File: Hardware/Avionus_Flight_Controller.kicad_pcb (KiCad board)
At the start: 4 copper layers, 101.6 x 101.6 mm, 285 parts, among them J1101 PPM, J1102 iBUS, J1201 S0, J1202 S1, J1203 S2, J1204 S3, J1205 S4, J1206 S5, J1207 S6, J1208 S7, J1209 S8, J1210 S9, J1211 S10, J1212 S11, J1213 S12, J1214 S13, J1215 S14, J1216 S15, J1401 LIDAR, J201 5V_SEL, J202 E5V, J203 POWER IN, J401 STDC14, J701 SD_Card, J801 USB_C_Receptacle_USB2.0, Q1101 RE1C002UN, Q1102 RE1C002UN, Q1201 RE1C002UN, Q1202 RE1C002UN, Q1203 RE1C002UN, Q1204 RE1C002UN, Q1205 RE1C002UN, Q1206 RE1C002UN, Q1207 RE1C002UN, Q1208 RE1C002UN, Q1209 RE1C002UN, Q1210 RE1C002UN, Q1211 RE1C002UN, Q1212 RE1C002UN, Q1213 RE1C002UN, Q1214 RE1C002UN, Q1215 RE1C002UN, Q1216 RE1C002UN, Q1301 RE1C002UN, Q1501 RE1C002UN, Q1502 RE1C002UN, Q1503 RE1C002UN, Q1504 RE1C002UN, Q1505 RE1C002UN, Q201 RE1C002UN, SW1301 SW_USER, SW201 START, SW301 RESET, U1001 MAX-M10S, U1101 USBLC6-4SC6, U1201 USBLC6-4SC6, U1202 USBLC6-4SC6, U1203 USBLC6-4SC6, U1204 USBLC6-4SC6, U1401 USBLC6-4SC6, U1501 ICM-20948, U201 AP2112K-3.3, U202 AOZ1212AI, U203 AP2151W, U204 AP2112K-3.3, U205 AP2112K-1.8, U206 AP2112K-3.3, U207 AP2112K-3.3, U208 ACS714xLCTR-50A, U209 ACS714xLCTR-50A, U210 AP2171W, U301 STM32F722ZETx, U401 USBLC6-4SC6, U402 USBLC6-4SC6, U501 W25Q128JVS, U502 W25Q128JVPM, U601 W25Q128JVS, U602 W25Q128JVPM, U801 USBLC6-2SC6, U901 LAMBDA62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

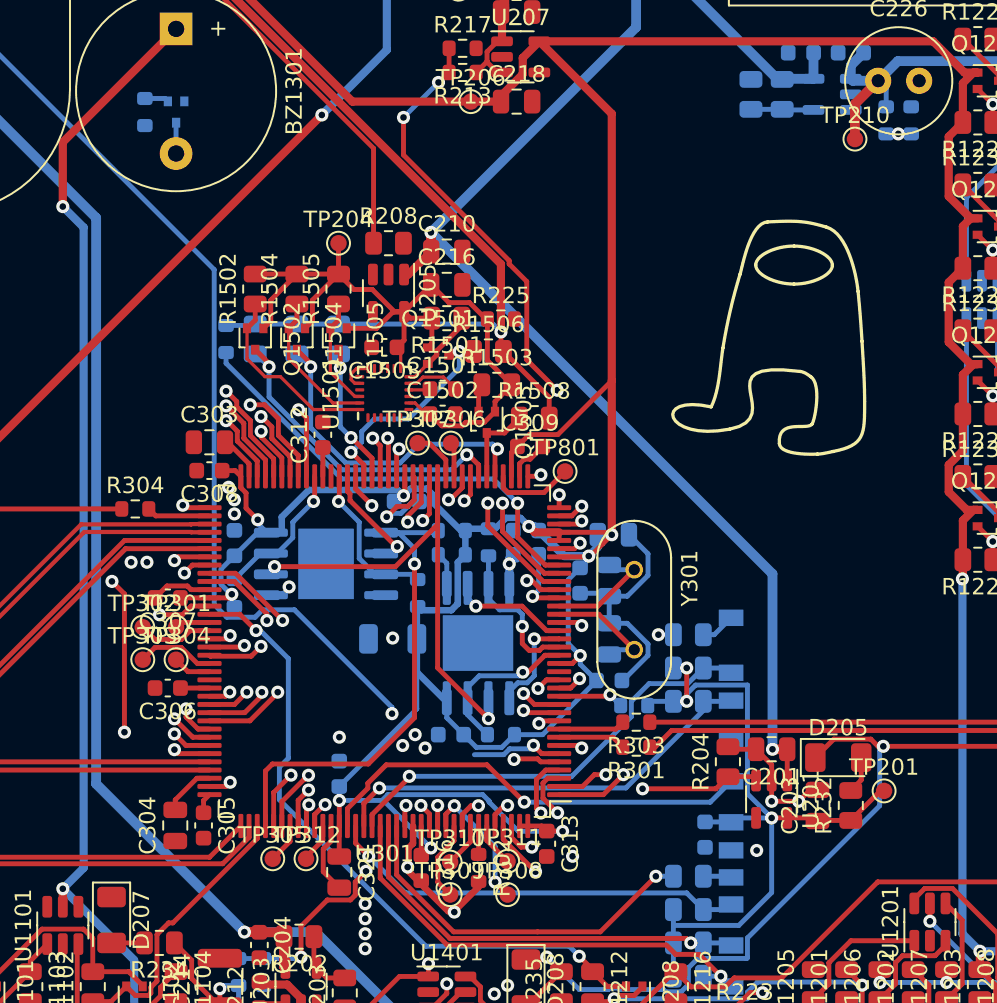
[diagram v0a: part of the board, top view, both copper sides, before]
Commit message: Schematic layout fixes
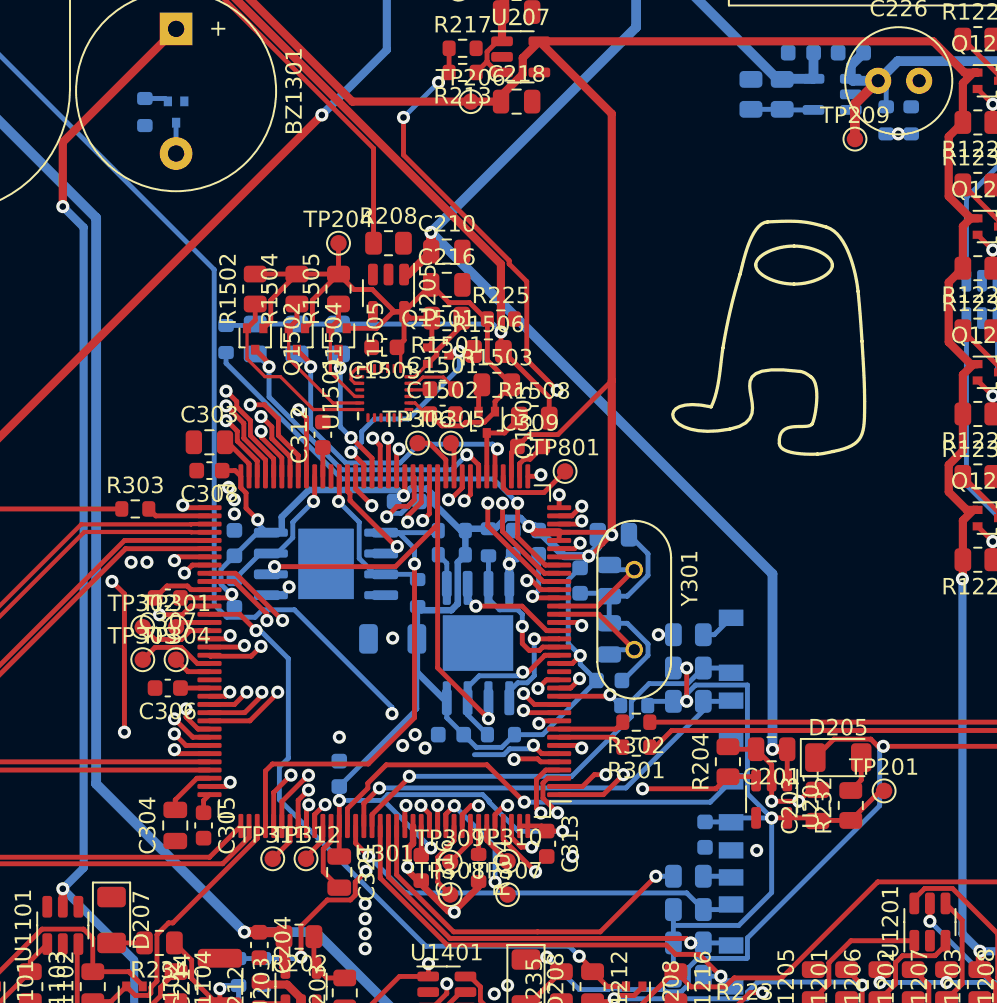
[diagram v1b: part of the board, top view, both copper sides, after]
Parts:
- renumbered R303 to R302, R304 to R303, R302 to R304, TP210 to TP209, TP306 to TP305, TP307 to TP306, TP308 to TP307, TP309 to TP308, TP310 to TP309, TP311 to TP310, TP305 to TP311
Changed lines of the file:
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@@
     (property "ki_keywords" "test point tp")
     (attr exclude_from_pos_files)
-    (fp_text reference "TP311" (at 0 -1.448) (layer "F.SilkS")
+    (fp_text reference "TP310" (at 0 -1.448) (layer "F.SilkS")
         (effects (font (size 1 1) (thickness 0.15)))
     )
@@
     (property "ki_keywords" "test point tp")
     (attr exclude_from_pos_files)
-    (fp_text reference "TP308" (at 0 -1.448) (layer "F.SilkS")
+    (fp_text reference "TP307" (at 0 -1.448) (layer "F.SilkS")
         (effects (font (size 1 1) (thickness 0.15)))
     )
@@
     (property "ki_keywords" "R resistor")
     (attr smd)
-    (fp_text reference "R304" (at 0 -1.43) (layer "F.SilkS")
+    (fp_text reference "R303" (at 0 -1.43) (layer "F.SilkS")
         (effects (font (size 1 1) (thickness 0.15)))
     )
@@
     (property "ki_keywords" "R resistor")
     (attr smd)
-    (fp_text reference "R302" (at 0 -1.43 -270) (layer "F.SilkS")
+    (fp_text reference "R304" (at 0 -1.43 -270) (layer "F.SilkS")
         (effects (font (size 1 1) (thickness 0.15)))
     )
@@
     (property "ki_keywords" "test point tp")
     (attr exclude_from_pos_files)
-    (fp_text reference "TP309" (at 0 -1.448) (layer "F.SilkS")
+    (fp_text reference "TP308" (at 0 -1.448) (layer "F.SilkS")
         (effects (font (size 1 1) (thickness 0.15)))
     )
@@
     (property "ki_keywords" "test point tp")
     (attr exclude_from_pos_files)
-    (fp_text reference "TP306" (at 0 -1.448) (layer "F.SilkS")
+    (fp_text reference "TP305" (at 0 -1.448) (layer "F.SilkS")
         (effects (font (size 1 1) (thickness 0.15)))
     )
@@
     (property "ki_keywords" "test point tp")
     (attr exclude_from_pos_files)
-    (fp_text reference "TP310" (at 0 -1.448) (layer "F.SilkS")
+    (fp_text reference "TP309" (at 0 -1.448) (layer "F.SilkS")
         (effects (font (size 1 1) (thickness 0.15)))
     )
@@
     (property "ki_keywords" "R resistor")
     (attr smd)
-    (fp_text reference "R303" (at 0 -1.43) (layer "F.SilkS")
+    (fp_text reference "R302" (at 0 -1.43) (layer "F.SilkS")
         (effects (font (size 1 1) (thickness 0.15)))
     )
@@
     (property "ki_keywords" "test point tp")
     (attr exclude_from_pos_files)
-    (fp_text reference "TP305" (at 0 -1.448) (layer "F.SilkS")
+    (fp_text reference "TP311" (at 0 -1.448) (layer "F.SilkS")
         (effects (font (size 1 1) (thickness 0.15)))
     )
@@
     (property "ki_keywords" "test point tp")
     (attr exclude_from_pos_files)
-    (fp_text reference "TP307" (at 0 -1.448) (layer "F.SilkS")
+    (fp_text reference "TP306" (at 0 -1.448) (layer "F.SilkS")
         (effects (font (size 1 1) (thickness 0.15)))
     )
@@
     (property "ki_keywords" "test point tp")
     (attr exclude_from_pos_files)
-    (fp_text reference "TP210" (at 0 -1.448) (layer "F.SilkS")
+    (fp_text reference "TP209" (at 0 -1.448) (layer "F.SilkS")
         (effects (font (size 1 1) (thickness 0.15)))
     )

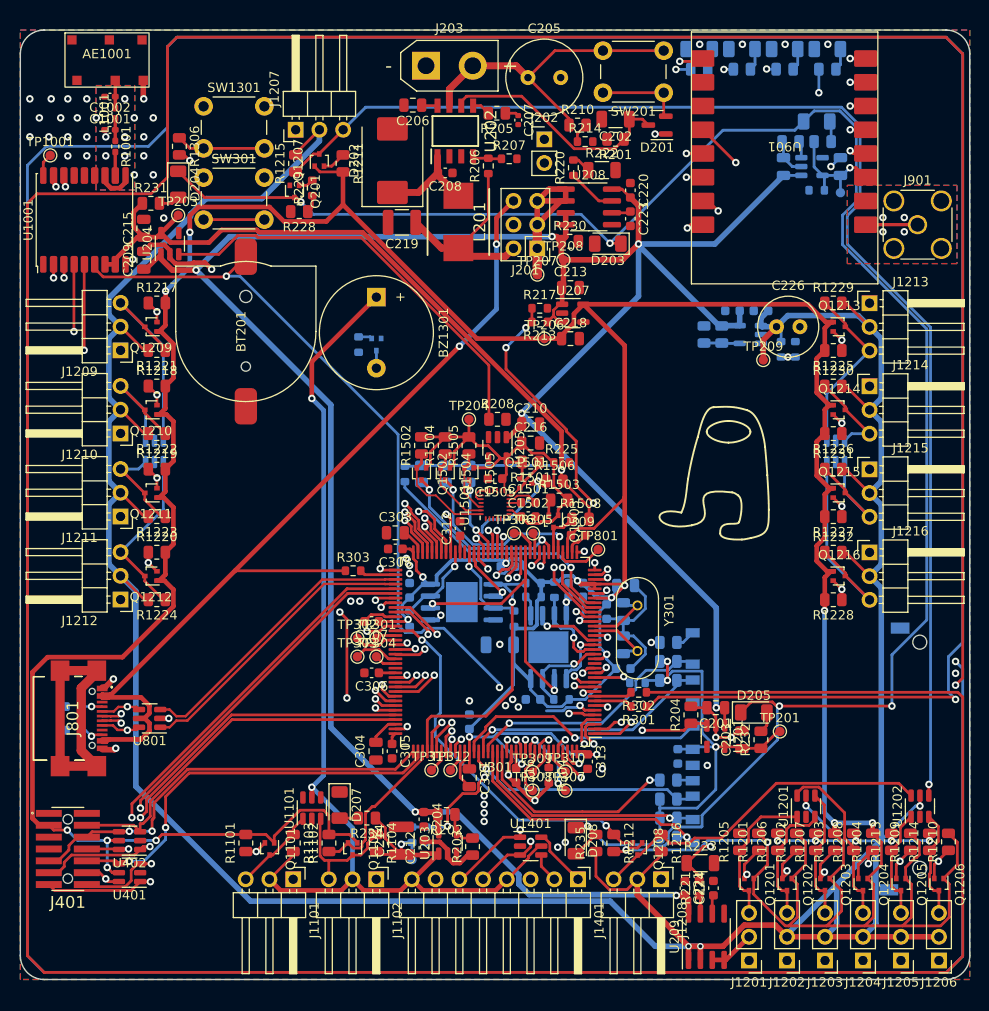
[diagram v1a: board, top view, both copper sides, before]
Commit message: Finalize routing
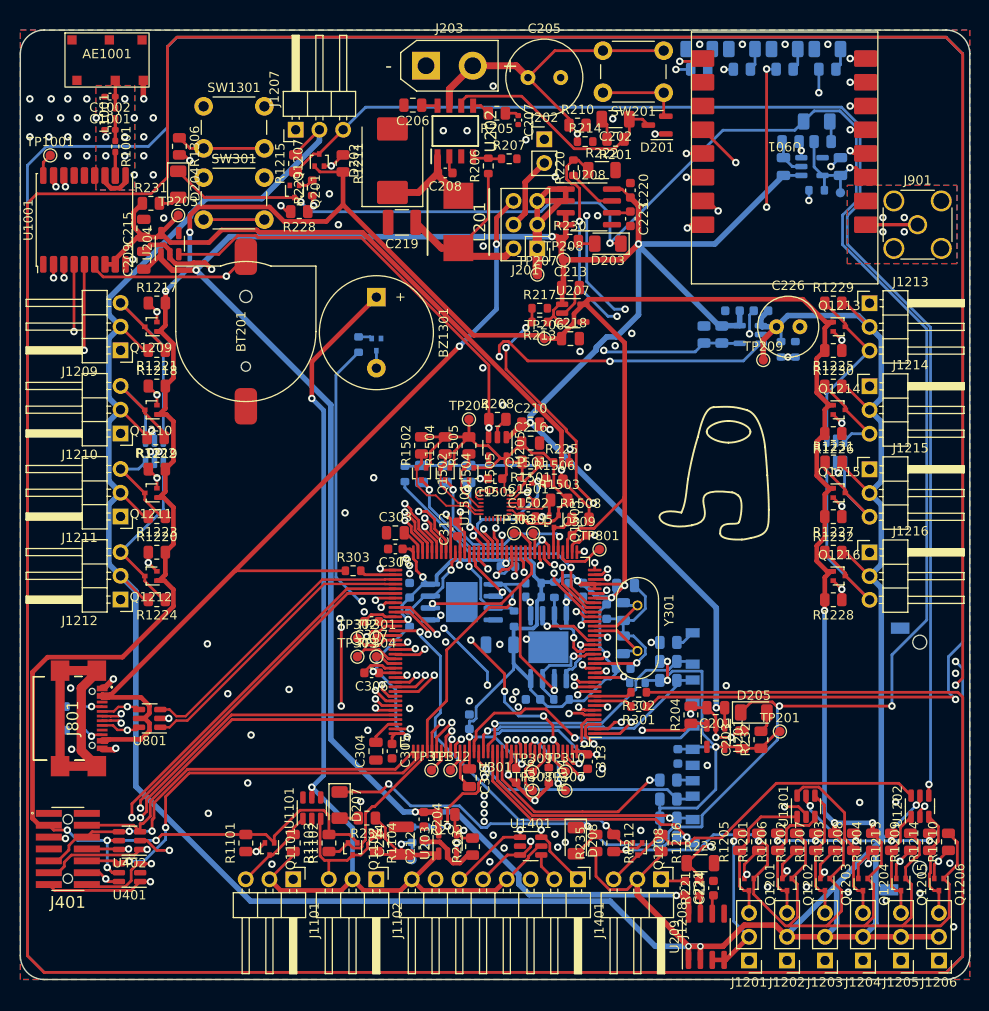
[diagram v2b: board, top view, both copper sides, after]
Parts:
- moved R1231 0.76 mm to (112.4, 71.6)
- moved R1222 0.47 mm to (39.9, 69.0)
- moved C312 0.27 mm to (72.2, 78.8)
- moved TP801 0.15 mm to (87.4, 81.0)
- moved C309 0.10 mm to (85.2, 79.5)
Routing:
- net /MCU/GPIO_PE3: track 4.18 -> 93.8 mm, vias 2 -> 4
- net /MCU/RTC_OUT: track 2.60 -> 89.2 mm
- net /MCU/ADC3_IN14: track 1.50 -> 77.1 mm, vias 1 -> 2
- net /MCU/GPIO_PG6+EXTI6: track 3.42 -> 77.6 mm, vias 1 -> 3
- net /MCU/GPIO_PG5: track 6.00 -> 72.0 mm, vias 1 -> 4
- net /MCU/GPIO_PG4: track 3.26 -> 67.6 mm, vias 1 -> 2
- net /SERVO/CH6: track 5.81 -> 70.2 mm, vias 1 -> 2
- net /MCU/GPIO_PF12: track 4.94 -> 66.8 mm, vias 1 -> 2
- net /MCU/ADC2_IN10: track 4.36 -> 63.7 mm, vias 1 -> 5
- net /MCU/TIM11_CH1: track 1.70 -> 60.3 mm, vias 1 -> 5
- net /MCU/ADC2_IN11: track 9.18 -> 59.4 mm, vias 1 -> 3
- net GND: track 91.7 -> 133.0 mm, vias 59 -> 117
- net Net-(D203-K): track 200.5 -> 232.2 mm, vias 5 -> 6
- net /MCU/ADC3_IN8: track 1.46 -> 29.2 mm, vias 1 -> 2
- net /GPS/SDA: track 95.3 -> 119.5 mm
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
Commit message: Misc fixes
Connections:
- R1305 pad 1: /UI/LED_GPS -> /MCU/GPIO_PE2
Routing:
- net /MCU/GPIO_PE2: track 4.42 -> 96.3 mm, vias 1 -> 4
- net GND: track 133.0 -> 161.4 mm, vias 117 -> 120
- net /UI/LED_GPS: track 2.52 -> 0.00 mm, vias 1 -> 0
- net /GPS/TXD: track 79.1 -> 80.3 mm
- net /GPS/EXTINT: track 81.9 -> 80.9 mm
- net /MCU/TIM11_CH1: vias 5 -> 4
- net /MCU/GPIO_PG5: vias 4 -> 3
